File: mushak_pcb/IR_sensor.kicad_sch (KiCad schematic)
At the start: 32 parts, among them J6 IR_1, J7 IR_3, J8 IR_2, J9 IR_4, Q2 DMN3065LW-7, Q3 DMN3065LW-7, Q4 DMN3065LW-7, Q5 DMN3065LW-7

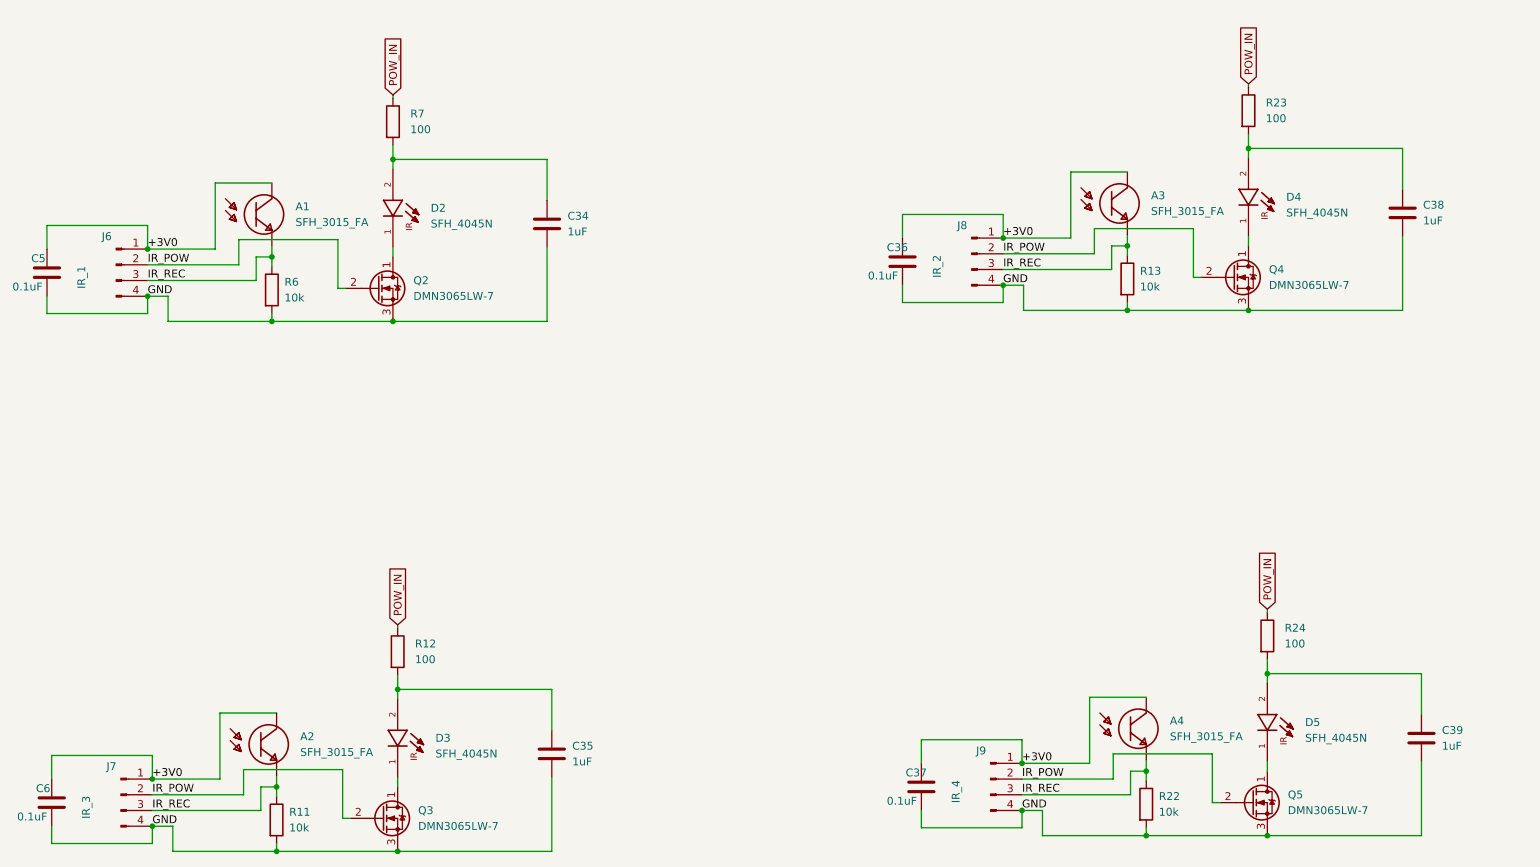
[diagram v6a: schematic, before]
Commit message: Completed sensor routing
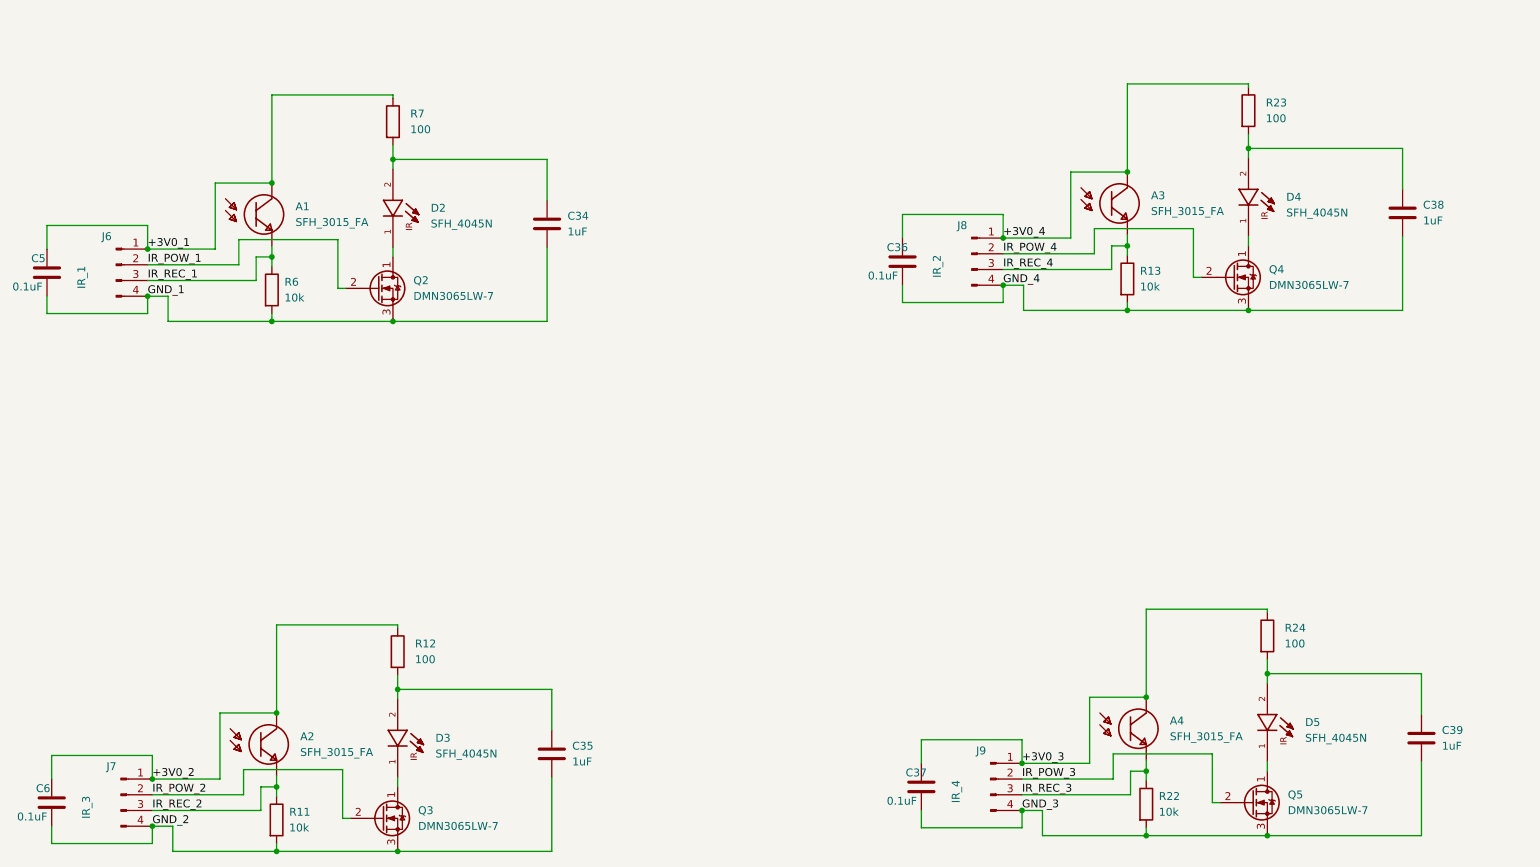
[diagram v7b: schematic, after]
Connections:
- removed net +3V0: A1.2, A2.2, A3.2, A4.2, C36.1, C37.1, C5.1, C6.1, J6.1 (Pin_1), J7.1 (Pin_1), J8.1 (Pin_1), J9.1 (Pin_1)
- removed net GND: C34.2, C35.2, C36.2, C37.2, C38.2, C39.2, C5.2, C6.2, J6.4 (Pin_4), J7.4 (Pin_4), J8.4 (Pin_4), J9.4 (Pin_4), Q2.3 (S), Q3.3 (S), Q4.3 (S), Q5.3 (S), R11.2, R13.2, R22.2, R6.2
- removed net IR_POW: J6.2 (Pin_2), J7.2 (Pin_2), J8.2 (Pin_2), J9.2 (Pin_2), Q2.2 (G), Q3.2 (G), Q4.2 (G), Q5.2 (G)
- removed net IR_REC: A1.1, A2.1, A3.1, A4.1, J6.3 (Pin_3), J7.3 (Pin_3), J8.3 (Pin_3), J9.3 (Pin_3), R11.1, R13.1, R22.1, R6.1
- removed net POW_IN: R12.1, R23.1, R24.1, R7.1
- new net +3V0_1: A1.2, C5.1, J6.1 (Pin_1), R7.1
- new net +3V0_2: A2.2, C6.1, J7.1 (Pin_1), R12.1
- new net +3V0_3: A4.2, C37.1, J9.1 (Pin_1), R24.1
- new net +3V0_4: A3.2, C36.1, J8.1 (Pin_1), R23.1
- new net GND_1: C34.2, C5.2, J6.4 (Pin_4), Q2.3 (S), R6.2
- new net GND_2: C35.2, C6.2, J7.4 (Pin_4), Q3.3 (S), R11.2
- new net GND_3: C37.2, C39.2, J9.4 (Pin_4), Q5.3 (S), R22.2
- new net GND_4: C36.2, C38.2, J8.4 (Pin_4), Q4.3 (S), R13.2
- new net IR_POW_1: J6.2 (Pin_2), Q2.2 (G)
- new net IR_POW_2: J7.2 (Pin_2), Q3.2 (G)
- new net IR_POW_3: J9.2 (Pin_2), Q5.2 (G)
- new net IR_POW_4: J8.2 (Pin_2), Q4.2 (G)
- new net IR_REC_1: A1.1, J6.3 (Pin_3), R6.1
- new net IR_REC_2: A2.1, J7.3 (Pin_3), R11.1
- new net IR_REC_3: A4.1, J9.3 (Pin_3), R22.1
- new net IR_REC_4: A3.1, J8.3 (Pin_3), R13.1
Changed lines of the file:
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@@
   (junction (at 64.008 63.754) (diameter 0) (color 0 0 0 0)
   )
+  (junction (at 64.77 137.414) (diameter 0) (color 0 0 0 0)
+  )
   (junction (at 224.79 157.226) (diameter 0) (color 0 0 0 0)
   )
+  (junction (at 205.232 134.874) (diameter 0) (color 0 0 0 0)
+  )
   (junction (at 43.942 70.104) (diameter 0) (color 0 0 0 0)
   )
@@
   (junction (at 43.942 62.484) (diameter 0) (color 0 0 0 0)
   )
+  (junction (at 64.008 51.816) (diameter 0) (color 0 0 0 0)
+  )
   (junction (at 202.184 61.976) (diameter 0) (color 0 0 0 0)
   )
@@
   (junction (at 84.328 159.766) (diameter 0) (color 0 0 0 0)
   )
+  (junction (at 202.184 50.038) (diameter 0) (color 0 0 0 0)
+  )
   (wire (pts (xy 64.77 149.352) (xy 64.77 150.876))
     (stroke (width 0) (type default) (color 0 0 0 0))
@@
     (stroke (width 0) (type default) (color 0 0 0 0))
   )
+  (wire (pts (xy 202.184 50.038) (xy 202.184 35.814))
+    (stroke (width 0) (type default) (color 0 0 0 0))
+  )
   (wire (pts (xy 182.118 60.706) (xy 193.04 60.706))
     (stroke (width 0) (type default) (color 0 0 0 0))
@@
     (stroke (width 0) (type default) (color 0 0 0 0))
   )
+  (wire (pts (xy 64.008 51.816) (xy 64.008 37.592))
+    (stroke (width 0) (type default) (color 0 0 0 0))
+  )
   (wire (pts (xy 84.328 147.828) (xy 84.328 149.352))
     (stroke (width 0) (type default) (color 0 0 0 0))
@@
     (stroke (width 0) (type default) (color 0 0 0 0))
   )
+  (wire (pts (xy 205.232 120.65) (xy 224.79 120.65))
+    (stroke (width 0) (type default) (color 0 0 0 0))
+  )
   (wire (pts (xy 205.232 146.812) (xy 205.232 148.336))
     (stroke (width 0) (type default) (color 0 0 0 0))
@@
     (stroke (width 0) (type default) (color 0 0 0 0))
   )
+  (wire (pts (xy 64.77 123.19) (xy 84.328 123.19))
+    (stroke (width 0) (type default) (color 0 0 0 0))
+  )
   (wire (pts (xy 202.184 72.39) (xy 202.184 71.12))
     (stroke (width 0) (type default) (color 0 0 0 0))
@@
     (stroke (width 0) (type default) (color 0 0 0 0))
   )
+  (wire (pts (xy 205.232 134.874) (xy 205.232 120.65))
+    (stroke (width 0) (type default) (color 0 0 0 0))
+  )
   (wire (pts (xy 205.232 157.226) (xy 224.79 157.226))
     (stroke (width 0) (type default) (color 0 0 0 0))
@@
     (stroke (width 0) (type default) (color 0 0 0 0))
   )
+  (wire (pts (xy 64.008 37.592) (xy 83.566 37.592))
+    (stroke (width 0) (type default) (color 0 0 0 0))
+  )
   (wire (pts (xy 75.438 154.432) (xy 76.708 154.432))
     (stroke (width 0) (type default) (color 0 0 0 0))
@@
     (stroke (width 0) (type default) (color 0 0 0 0))
   )
+  (wire (pts (xy 64.77 137.414) (xy 64.77 123.19))
+    (stroke (width 0) (type default) (color 0 0 0 0))
+  )
   (wire (pts (xy 83.566 48.006) (xy 83.566 49.53))
     (stroke (width 0) (type default) (color 0 0 0 0))
@@
     (stroke (width 0) (type default) (color 0 0 0 0))
   )
+  (wire (pts (xy 202.184 35.814) (xy 221.742 35.814))
+    (stroke (width 0) (type default) (color 0 0 0 0))
+  )
   (wire (pts (xy 54.864 62.484) (xy 54.864 51.816))
     (stroke (width 0) (type default) (color 0 0 0 0))
@@
     (stroke (width 0) (type default) (color 0 0 0 0))
   )
-  (label "IR_REC" (at 44.704 153.162 0)
-    (effects (font (size 1.27 1.27)) (justify left bottom))
-  )
-  (label "+3V0" (at 182.118 60.706 0)
-    (effects (font (size 1.27 1.27)) (justify left bottom))
-  )
-  (label "IR_REC" (at 185.166 150.622 0)
-    (effects (font (size 1.27 1.27)) (justify left bottom))
-  )
-  (label "IR_REC" (at 182.118 65.786 0)
-    (effects (font (size 1.27 1.27)) (justify left bottom))
-  )
-  (label "IR_POW" (at 44.704 150.622 0)
-    (effects (font (size 1.27 1.27)) (justify left bottom))
-  )
-  (label "IR_POW" (at 185.166 148.082 0)
-    (effects (font (size 1.27 1.27)) (justify left bottom))
-  )
-  (label "GND" (at 185.166 153.162 0)
-    (effects (font (size 1.27 1.27)) (justify left bottom))
-  )
-  (label "GND" (at 182.118 68.326 0)
-    (effects (font (size 1.27 1.27)) (justify left bottom))
-  )
-  (label "+3V0" (at 43.942 62.484 0)
-    (effects (font (size 1.27 1.27)) (justify left bottom))
-  )
-  (label "GND" (at 43.942 70.104 0)
-    (effects (font (size 1.27 1.27)) (justify left bottom))
-  )
-  (label "GND" (at 44.704 155.702 0)
-    (effects (font (size 1.27 1.27)) (justify left bottom))
-  )
-  (label "+3V0" (at 185.166 145.542 0)
-    (effects (font (size 1.27 1.27)) (justify left bottom))
-  )
-  (label "IR_REC" (at 43.942 67.564 0)
-    (effects (font (size 1.27 1.27)) (justify left bottom))
-  )
-  (label "IR_POW" (at 43.942 65.024 0)
-    (effects (font (size 1.27 1.27)) (justify left bottom))
-  )
-  (label "IR_POW" (at 182.118 63.246 0)
-    (effects (font (size 1.27 1.27)) (justify left bottom))
-  )
-  (label "+3V0" (at 44.704 148.082 0)
-    (effects (font (size 1.27 1.27)) (justify left bottom))
-  )
-  (global_label "POW_IN" (shape input) (at 84.328 123.19 90) (fields_autoplaced)
-    (effects (font (size 1.27 1.27)) (justify left))
-    (property "Intersheet References" "${INTERSHEET_REFS}" (id 0) (at 84.4074 113.8221 90)
-      (effects (font (size 1.27 1.27)) (justify left) hide)
-    )
-  )
-  (global_label "POW_IN" (shape input) (at 83.566 37.592 90) (fields_autoplaced)
-    (effects (font (size 1.27 1.27)) (justify left))
-    (property "Intersheet References" "${INTERSHEET_REFS}" (id 0) (at 83.6454 28.2241 90)
-      (effects (font (size 1.27 1.27)) (justify left) hide)
-    )
-  )
-  (global_label "POW_IN" (shape input) (at 221.742 35.814 90) (fields_autoplaced)
-    (effects (font (size 1.27 1.27)) (justify left))
-    (property "Intersheet References" "${INTERSHEET_REFS}" (id 0) (at 221.8214 26.4461 90)
-      (effects (font (size 1.27 1.27)) (justify left) hide)
-    )
-  )
-  (global_label "POW_IN" (shape input) (at 224.79 120.65 90) (fields_autoplaced)
-    (effects (font (size 1.27 1.27)) (justify left))
-    (property "Intersheet References" "${INTERSHEET_REFS}" (id 0) (at 224.8694 111.2821 90)
-      (effects (font (size 1.27 1.27)) (justify left) hide)
-    )
+  (label "IR_REC_2" (at 44.704 153.162 0)
+    (effects (font (size 1.27 1.27)) (justify left bottom))
+  )
+  (label "+3V0_4" (at 182.118 60.706 0)
+    (effects (font (size 1.27 1.27)) (justify left bottom))
+  )
+  (label "IR_REC_3" (at 185.166 150.622 0)
+    (effects (font (size 1.27 1.27)) (justify left bottom))
+  )
+  (label "IR_REC_4" (at 182.118 65.786 0)
+    (effects (font (size 1.27 1.27)) (justify left bottom))
+  )
+  (label "IR_POW_2" (at 44.704 150.622 0)
+    (effects (font (size 1.27 1.27)) (justify left bottom))
+  )
+  (label "IR_POW_3" (at 185.166 148.082 0)
+    (effects (font (size 1.27 1.27)) (justify left bottom))
+  )
+  (label "GND_3" (at 185.166 153.162 0)
+    (effects (font (size 1.27 1.27)) (justify left bottom))
+  )
+  (label "GND_4" (at 182.118 68.326 0)
+    (effects (font (size 1.27 1.27)) (justify left bottom))
+  )
+  (label "+3V0_1" (at 43.942 62.484 0)
+    (effects (font (size 1.27 1.27)) (justify left bottom))
+  )
+  (label "GND_1" (at 43.942 70.104 0)
+    (effects (font (size 1.27 1.27)) (justify left bottom))
+  )
+  (label "GND_2" (at 44.704 155.702 0)
+    (effects (font (size 1.27 1.27)) (justify left bottom))
+  )
+  (label "+3V0_3" (at 185.166 145.542 0)
+    (effects (font (size 1.27 1.27)) (justify left bottom))
+  )
+  (label "IR_REC_1" (at 43.942 67.564 0)
+    (effects (font (size 1.27 1.27)) (justify left bottom))
+  )
+  (label "IR_POW_1" (at 43.942 65.024 0)
+    (effects (font (size 1.27 1.27)) (justify left bottom))
+  )
+  (label "IR_POW_4" (at 182.118 63.246 0)
+    (effects (font (size 1.27 1.27)) (justify left bottom))
+  )
+  (label "+3V0_2" (at 44.704 148.082 0)
+    (effects (font (size 1.27 1.27)) (justify left bottom))
   )
   (symbol (lib_id "SFH_4045N:SFH_4045N") (at 221.742 55.372 270) (unit 1)

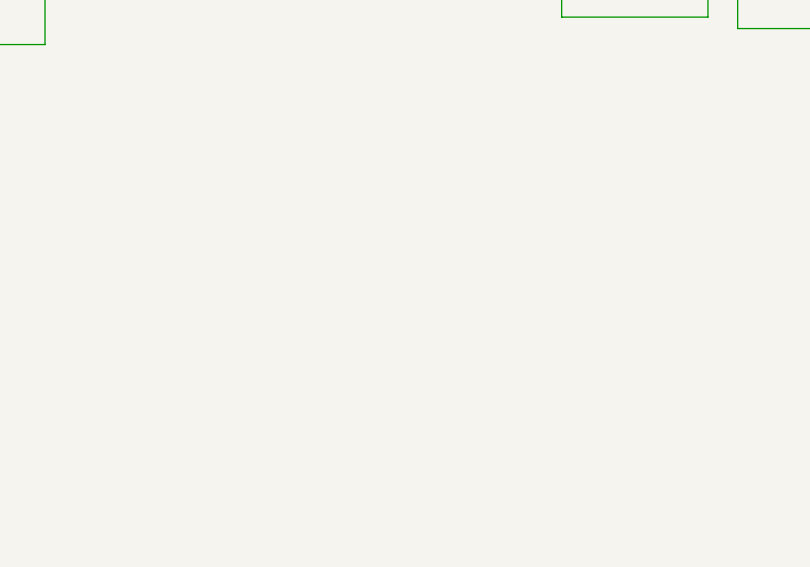
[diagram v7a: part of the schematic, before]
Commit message: changed oscilattor placement
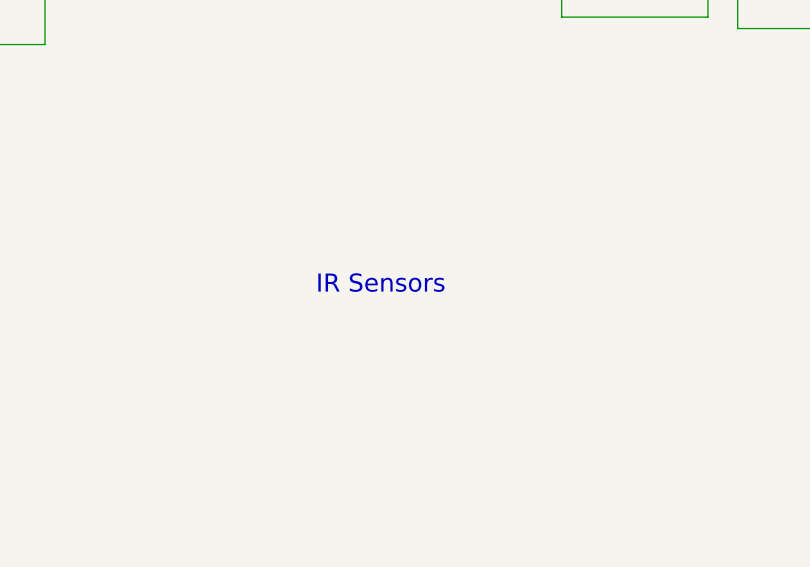
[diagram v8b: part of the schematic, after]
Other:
- note added: "IR Sensors"
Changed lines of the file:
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@@
     (stroke (width 0) (type default) (color 0 0 0 0))
+  )
+  (text "IR Sensors" (at 138.557 102.108 0)
+    (effects (font (size 2 2)) (justify left bottom))
   )
   (label "IR_REC_2" (at 44.704 153.162 0)
